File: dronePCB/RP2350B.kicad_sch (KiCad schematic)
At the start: 43 parts, among them J1 BM03B-SRSS-TB, J2 USB_C_Receptacle, SW1 SW_BOOT, SW2 SW_RESET, U1 RP2350_80QFN, U2 W25Q128JVPIQ, U3 APS6404L-3SQR-ZR, Y1 ABM8-272-T3

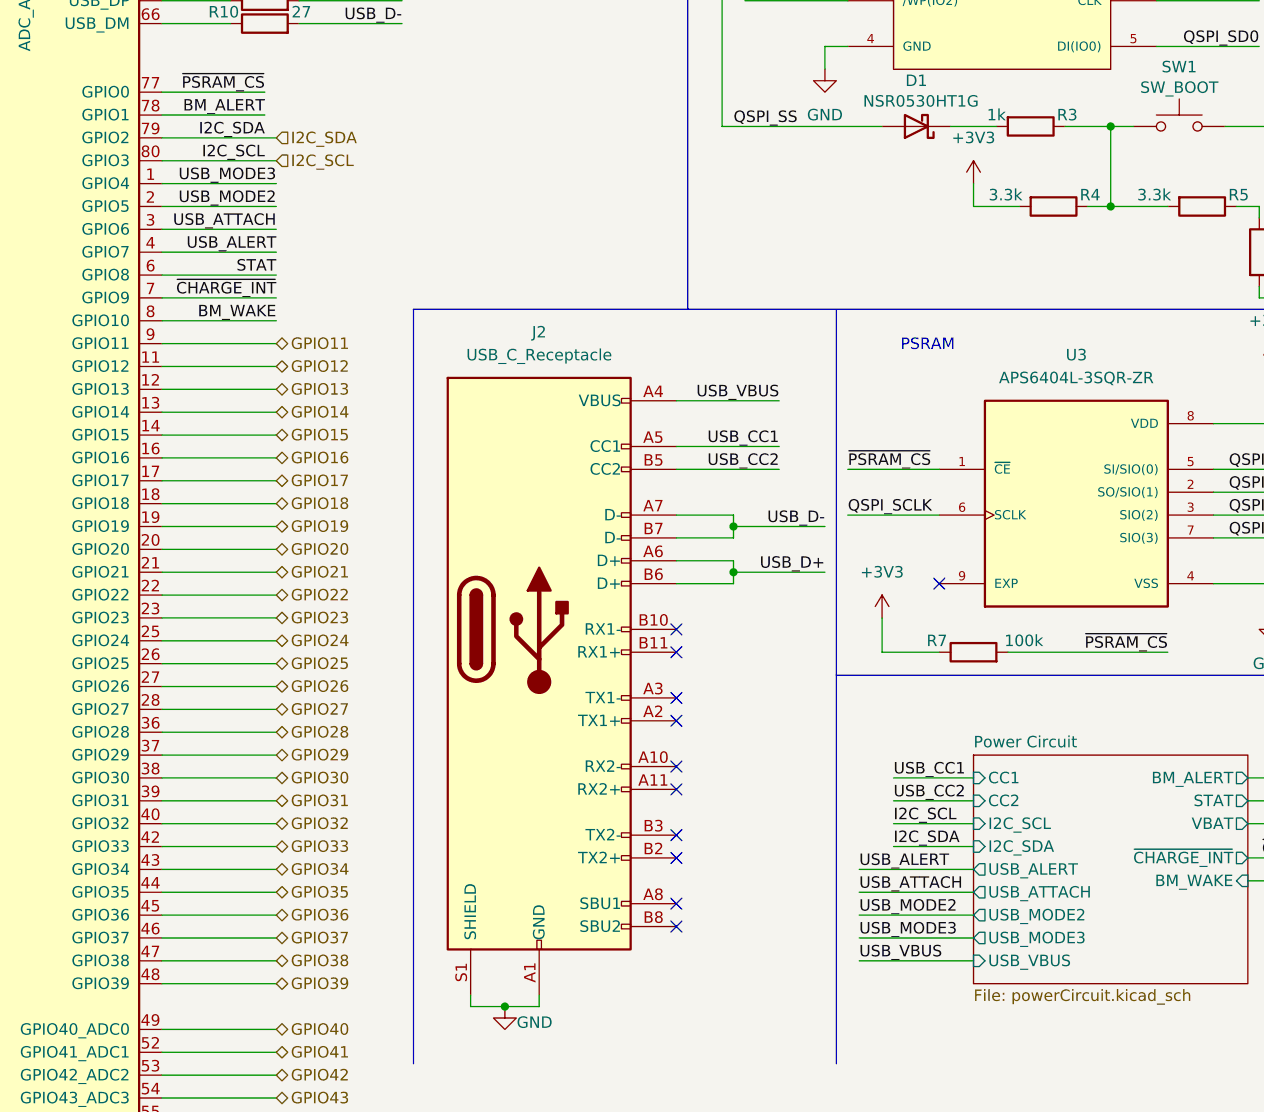
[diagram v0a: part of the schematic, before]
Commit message: Routed RP2350B w/ dependencies + power circuit
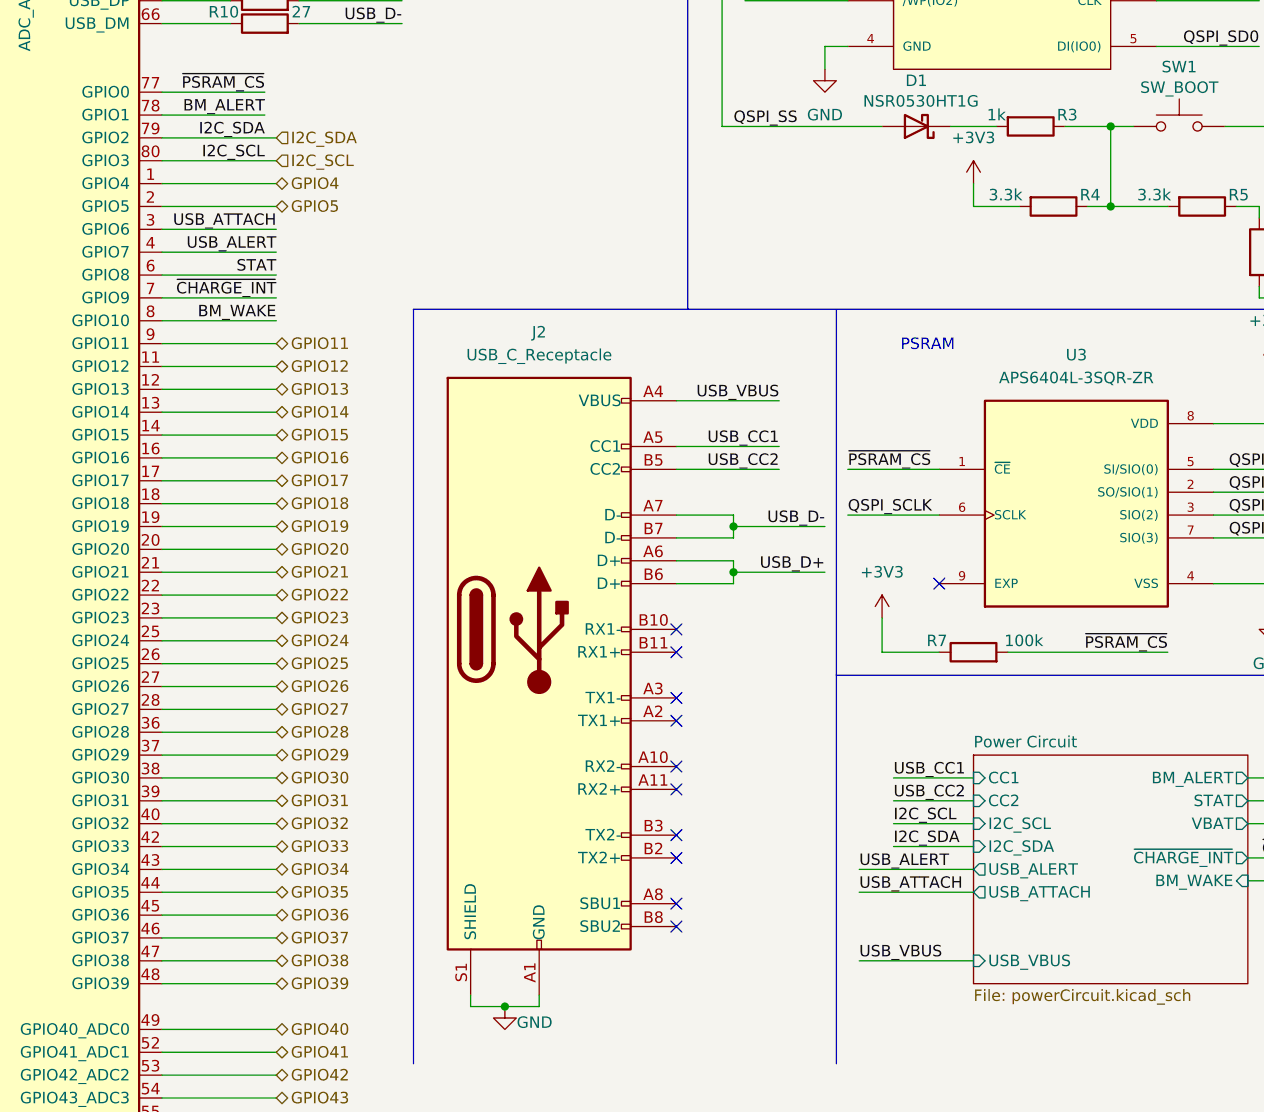
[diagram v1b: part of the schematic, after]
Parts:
- C1, C10, C11, C12, C13, C14, C15, C16, C17, C18, C19, C20, C21, C4, C5, C6, C7, C8, C9, R1, R10, R11, R12, R2, R3, R4, R5, R6, R7, R8, R9: footprint (none) -> Capacitor_SMD:C_0805_2012Metric_Pad1.18x1.45mm_HandSolder
- C2, C3: footprint (none) -> Capacitor_SMD:C_0504_1310Metric_Pad0.83x1.28mm_HandSolder
- D1: footprint (none) -> Diode_SMD:D_SOD-323_HandSoldering
- J1: footprint (none) -> Connector_JST:JST_PH_B2B-PH-SM4-TB_1x02-1MP_P2.00mm_Vertical
- J2: footprint (none) -> Connector_USB:USB_C_Receptacle_Amphenol_12401610E4-2A
- L1: footprint (none) -> droneParts:AOTAB201610S3R3101T
- SW1, SW2: footprint (none) -> Button_Switch_SMD:SW_Push_1P1T_NO_Vertical_Wuerth_434133025816
- U1: footprint RP2350_80QFN_minimal:RP2350-QFN-80-1EP_10x10_P0.4mm_EP3.4x3.4mm_ThermalVias -> MCU:RP2350B
- U2: footprint W25Q128JVPIQ:W25Q128JVPIQ -> Flash:W25Q128JVPIQ
- U3: footprint APS6404L-3SQR-ZR:PSON50P200X300X50-9N -> droneParts:PSON50P200X300X50-9N
- Y1: footprint (none) -> droneParts:ABM8272T3
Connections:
- net USB_MODE2 renamed GPIO5
- net USB_MODE3 renamed GPIO4
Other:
- sheet Power Circuit ports: added none; removed USB_MODE2, USB_MODE3
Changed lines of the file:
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@@
 	(wire
 		(pts
-			(xy 227.33 151.13) (xy 240.03 151.13)
-		)
-		(stroke
-			(width 0)
-			(type default)
-		)
-	)
-	(wire
-		(pts
 			(xy 81.28 50.8) (xy 63.5 50.8)
 		)
@@
 	(wire
 		(pts
-			(xy 227.33 148.59) (xy 240.03 148.59)
-		)
-		(stroke
-			(width 0)
-			(type default)
-		)
-	)
-	(wire
-		(pts
 			(xy 271.78 69.85) (xy 271.78 71.12)
 		)
@@
 		)
 	)
-	(label "USB_MODE2"
-		(at 227.33 148.59 0)
-		(effects
-			(font
-				(size 1.27 1.27)
-			)
-			(justify left bottom)
-		)
-	)
 	(label "QSPI_SD1"
 		(at 276.86 101.6 180)
@@
 		)
 	)
-	(label "USB_MODE2"
-		(at 162.56 69.85 180)
-		(effects
-			(font
-				(size 1.27 1.27)
-			)
-			(justify right bottom)
-		)
-	)
 	(label "QSPI_SS"
 		(at 69.85 68.58 0)
@@
 		)
 	)
-	(label "USB_MODE3"
-		(at 227.33 151.13 0)
-		(effects
-			(font
-				(size 1.27 1.27)
-			)
-			(justify left bottom)
-		)
-	)
-	(label "USB_MODE3"
-		(at 162.56 67.31 180)
-		(effects
-			(font
-				(size 1.27 1.27)
-			)
-			(justify right bottom)
-		)
-	)
 	(label "I2C_SCL"
 		(at 161.29 64.77 180)
@@
 		)
 	)
+	(hierarchical_label "GPIO5"
+		(shape bidirectional)
+		(at 162.56 69.85 0)
+		(effects
+			(font
+				(size 1.27 1.27)
+			)
+			(justify left)
+		)
+	)
 	(hierarchical_label "GPIO13"
 		(shape bidirectional)
@@
 		)
 	)
+	(hierarchical_label "GPIO4"
+		(shape bidirectional)
+		(at 162.56 67.31 0)
+		(effects
+			(font
+				(size 1.27 1.27)
+			)
+			(justify left)
+		)
+	)
 	(hierarchical_label "GPIO14"
 		(shape bidirectional)
@@
 			)
 		)
-		(property "Footprint" ""
+		(property "Footprint" "Capacitor_SMD:C_0805_2012Metric_Pad1.18x1.45mm_HandSolder"
 			(at 161.29 48.768 90)
 			(effects
@@
 			)
 		)
-		(property "Footprint" ""
+		(property "Footprint" "Capacitor_SMD:C_0805_2012Metric_Pad1.18x1.45mm_HandSolder"
 			(at 280.3652 97.79 0)
 			(effects
@@
 			)
 		)
-		(property "Footprint" ""
+		(property "Footprint" "Capacitor_SMD:C_0805_2012Metric_Pad1.18x1.45mm_HandSolder"
 			(at 144.4752 27.94 0)
 			(effects
@@
 			)
 		)
-		(property "Footprint" "APS6404L-3SQR-ZR:PSON50P200X300X50-9N"
+		(property "Footprint" "droneParts:PSON50P200X300X50-9N"
 			(at 251.46 101.6 0)
 			(effects
@@
 			)
 		)
-		(property "Footprint" ""
+		(property "Footprint" "Capacitor_SMD:C_0805_2012Metric_Pad1.18x1.45mm_HandSolder"
 			(at 220.472 25.4 90)
 			(effects
@@
 			)
 		)
-		(property "Footprint" ""
+		(property "Footprint" "droneParts:ABM8272T3"
 			(at 41.91 93.98 0)
 			(effects
@@
 			)
 		)
-		(property "Footprint" ""
+		(property "Footprint" "Capacitor_SMD:C_0805_2012Metric_Pad1.18x1.45mm_HandSolder"
 			(at 280.3652 33.02 0)
 			(effects
@@
 			)
 		)
-		(property "Footprint" ""
+		(property "Footprint" "Capacitor_SMD:C_0805_2012Metric_Pad1.18x1.45mm_HandSolder"
 			(at 29.21 187.198 90)
 			(effects
@@
 			)
 		)
-		(property "Footprint" ""
+		(property "Footprint" "Capacitor_SMD:C_0805_2012Metric_Pad1.18x1.45mm_HandSolder"
 			(at 56.8452 46.99 0)
 			(effects
@@
 			)
 		)
-		(property "Footprint" ""
+		(property "Footprint" "Capacitor_SMD:C_0805_2012Metric_Pad1.18x1.45mm_HandSolder"
 			(at 265.43 68.072 90)
 			(effects
@@
 			)
 		)
-		(property "Footprint" ""
+		(property "Footprint" "Capacitor_SMD:C_0805_2012Metric_Pad1.18x1.45mm_HandSolder"
 			(at 157.1752 27.94 0)
 			(effects
@@
 			)
 		)
-		(property "Footprint" ""
+		(property "Footprint" "Capacitor_SMD:C_0805_2012Metric_Pad1.18x1.45mm_HandSolder"
 			(at 195.2752 27.94 0)
 			(effects
@@
 			)
 		)
-		(property "Footprint" "RP2350_80QFN_minimal:RP2350-QFN-80-1EP_10x10_P0.4mm_EP3.4x3.4mm_ThermalVias"
+		(property "Footprint" "MCU:RP2350B"
 			(at 93.98 90.17 0)
 			(effects
@@
 			)
 		)
-		(property "Footprint" ""
+		(property "Footprint" "Capacitor_SMD:C_0805_2012Metric_Pad1.18x1.45mm_HandSolder"
 			(at 248.92 68.072 90)
 			(effects
@@
 			)
 		)
-		(property "Footprint" ""
+		(property "Footprint" "Connector_USB:USB_C_Receptacle_Amphenol_12401610E4-2A"
 			(at 195.58 116.84 0)
 			(effects
@@
 			)
 		)
-		(property "Footprint" ""
+		(property "Footprint" "Capacitor_SMD:C_0805_2012Metric_Pad1.18x1.45mm_HandSolder"
 			(at 176.2252 27.94 0)
 			(effects
@@
 			)
 		)
-		(property "Footprint" ""
+		(property "Footprint" "Capacitor_SMD:C_0805_2012Metric_Pad1.18x1.45mm_HandSolder"
 			(at 270.002 74.93 90)
 			(effects
@@
 			)
 		)
-		(property "Footprint" ""
+		(property "Footprint" "Capacitor_SMD:C_0805_2012Metric_Pad1.18x1.45mm_HandSolder"
 			(at 31.75 87.9348 0)
 			(effects
@@
 			)
 		)
-		(property "Footprint" ""
+		(property "Footprint" "Connector_JST:JST_PH_B2B-PH-SM4-TB_1x02-1MP_P2.00mm_Vertical"
 			(at 22.86 160.02 0)
 			(effects
@@
 			)
 		)
-		(property "Footprint" ""
+		(property "Footprint" "Capacitor_SMD:C_0805_2012Metric_Pad1.18x1.45mm_HandSolder"
 			(at 188.9252 27.94 0)
 			(effects
@@
 			)
 		)
-		(property "Footprint" ""
+		(property "Footprint" "Capacitor_SMD:C_0805_2012Metric_Pad1.18x1.45mm_HandSolder"
 			(at 72.0852 27.94 0)
 			(effects
@@
 			)
 		)
-		(property "Footprint" ""
+		(property "Footprint" "Capacitor_SMD:C_0805_2012Metric_Pad1.18x1.45mm_HandSolder"
 			(at 31.75 98.0948 0)
 			(effects
@@
 			)
 		)
-		(property "Footprint" ""
+		(property "Footprint" "Capacitor_SMD:C_0805_2012Metric_Pad1.18x1.45mm_HandSolder"
 			(at 29.21 191.008 90)
 			(effects
@@
 			)
 		)
-		(property "Footprint" "W25Q128JVPIQ:W25Q128JVPIQ"
+		(property "Footprint" "Flash:W25Q128JVPIQ"
 			(at 242.57 44.45 0)
 			(effects
@@
 			)
 		)
-		(property "Footprint" ""
+		(property "Footprint" "Capacitor_SMD:C_0805_2012Metric_Pad1.18x1.45mm_HandSolder"
 			(at 161.29 51.308 90)
 			(effects
@@
 			)
 		)
-		(property "Footprint" ""
+		(property "Footprint" "Capacitor_SMD:C_0805_2012Metric_Pad1.18x1.45mm_HandSolder"
 			(at 240.03 121.158 90)
 			(effects
@@
 			)
 		)
-		(property "Footprint" ""
+		(property "Footprint" "Button_Switch_SMD:SW_Push_1P1T_NO_Vertical_Wuerth_434133025816"
 			(at 66.04 105.41 0)
 			(effects
@@
 			)
 		)
-		(property "Footprint" ""
+		(property "Footprint" "Capacitor_SMD:C_0504_1310Metric_Pad0.83x1.28mm_HandSolder"
 			(at 26.3652 57.15 0)
 			(effects
@@
 			)
 		)
-		(property "Footprint" ""
+		(property "Footprint" "Capacitor_SMD:C_0805_2012Metric_Pad1.18x1.45mm_HandSolder"
 			(at 246.38 59.182 90)
 			(effects
@@
 			)
 		)
-		(property "Footprint" ""
+		(property "Footprint" "Capacitor_SMD:C_0805_2012Metric_Pad1.18x1.45mm_HandSolder"
 			(at 150.8252 27.94 0)
 			(effects
@@
 			)
 		)
-		(property "Footprint" ""
+		(property "Footprint" "Button_Switch_SMD:SW_Push_1P1T_NO_Vertical_Wuerth_434133025816"
 			(at 262.89 55.88 0)
 			(effects
@@
 			)
 		)
-		(property "Footprint" ""
+		(property "Footprint" "Capacitor_SMD:C_0805_2012Metric_Pad1.18x1.45mm_HandSolder"
 			(at 60.96 100.838 90)
 			(effects
@@
 			)
 		)
-		(property "Footprint" ""
+		(property "Footprint" "Capacitor_SMD:C_0805_2012Metric_Pad1.18x1.45mm_HandSolder"
 			(at 84.7852 27.94 0)
 			(effects
@@
 			)
 		)
-		(property "Footprint" ""
+		(property "Footprint" "Capacitor_SMD:C_0805_2012Metric_Pad1.18x1.45mm_HandSolder"
 			(at 182.5752 27.94 0)
 			(effects
@@
 			)
 		)
-		(property "Footprint" ""
+		(property "Footprint" "Capacitor_SMD:C_0805_2012Metric_Pad1.18x1.45mm_HandSolder"
 			(at 78.4352 27.94 0)
 			(effects
@@
 			)
 		)
-		(property "Footprint" ""
+		(property "Footprint" "Capacitor_SMD:C_0805_2012Metric_Pad1.18x1.45mm_HandSolder"
 			(at 46.99 36.322 90)
 			(effects
@@
 			)
 		)
-		(property "Footprint" ""
+		(property "Footprint" "Capacitor_SMD:C_0805_2012Metric_Pad1.18x1.45mm_HandSolder"
 			(at 201.6252 27.94 0)
 			(effects
@@
 			)
 		)
-		(property "Footprint" ""
+		(property "Footprint" "Capacitor_SMD:C_0805_2012Metric_Pad1.18x1.45mm_HandSolder"
 			(at 138.1252 27.94 0)
 			(effects
@@
 			)
 		)
-		(property "Footprint" ""
+		(property "Footprint" "Capacitor_SMD:C_0805_2012Metric_Pad1.18x1.45mm_HandSolder"
 			(at 169.8752 27.94 0)
 			(effects
@@
 			)
 		)
-		(property "Footprint" ""
+		(property "Footprint" "Capacitor_SMD:C_0805_2012Metric_Pad1.18x1.45mm_HandSolder"
 			(at 163.5252 27.94 0)
 			(effects
@@
 			)
 		)
-		(property "Footprint" ""
+		(property "Footprint" "Capacitor_SMD:C_0504_1310Metric_Pad0.83x1.28mm_HandSolder"
 			(at 36.5252 57.15 0)
 			(effects
@@
 			)
 		)
-		(property "Footprint" ""
+		(property "Footprint" "Diode_SMD:D_SOD-323_HandSoldering"
 			(at 233.68 60.96 0)
 			(effects
@@
 			)
 		)
-		(property "Footprint" ""
+		(property "Footprint" "droneParts:AOTAB201610S3R3101T"
 			(at 44.45 53.34 0)
 			(effects
@@
 			(effects
 				(font
-					(size 1.27 1.27)
-				)
-				(justify left)
-			)
-		)
-		(pin "USB_MODE2" output
-			(at 240.03 148.59 180)
-			(effects
-				(font
-					(size 1.27 1.27)
-				)
-				(justify left)
-			)
-		)
-		(pin "USB_MODE3" output
-			(at 240.03 151.13 180)
-			(effects
-				(font

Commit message: Finished PCB
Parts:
- J1: footprint Connector_JST:JST_PH_B2B-PH-SM4-TB_1x02-1MP_P2.00mm_Vertical -> Connector_JST:JST_SH_BM03B-SRSS-TB_1x03-1MP_P1.00mm_Vertical
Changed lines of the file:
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@@
 			)
 		)
-		(property "Footprint" "Connector_JST:JST_PH_B2B-PH-SM4-TB_1x02-1MP_P2.00mm_Vertical"
+		(property "Footprint" "Connector_JST:JST_SH_BM03B-SRSS-TB_1x03-1MP_P1.00mm_Vertical"
 			(at 22.86 160.02 0)
 			(effects
